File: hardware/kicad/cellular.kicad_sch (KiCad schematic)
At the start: 41 parts, among them J4 SMN-304, Q3 S8050, Q4 S8050, Q5 PMBT3904, Q6 PMBT3904, U9 A7670C

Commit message: GNSS and Antenna Update
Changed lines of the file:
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@@
-	(wire
-		(pts
-			(xy 178.435 20.955) (xy 181.61 20.955)
-		)
-		(stroke
-			(width 0)
-			(type default)
-		)
-	)
 	(wire
 		(pts
@@
 	(wire
 		(pts
-			(xy 181.61 20.955) (xy 181.61 30.48)
+			(xy 181.61 22.86) (xy 181.61 30.48)
 		)
 		(stroke
@@
 	(hierarchical_label "CELL_BATT"
 		(shape input)
-		(at 178.435 20.955 180)
-		(fields_autoplaced yes)
-		(effects
+		(at 181.61 22.86 180)
+		(fields_autoplaced yes)
+		(effects

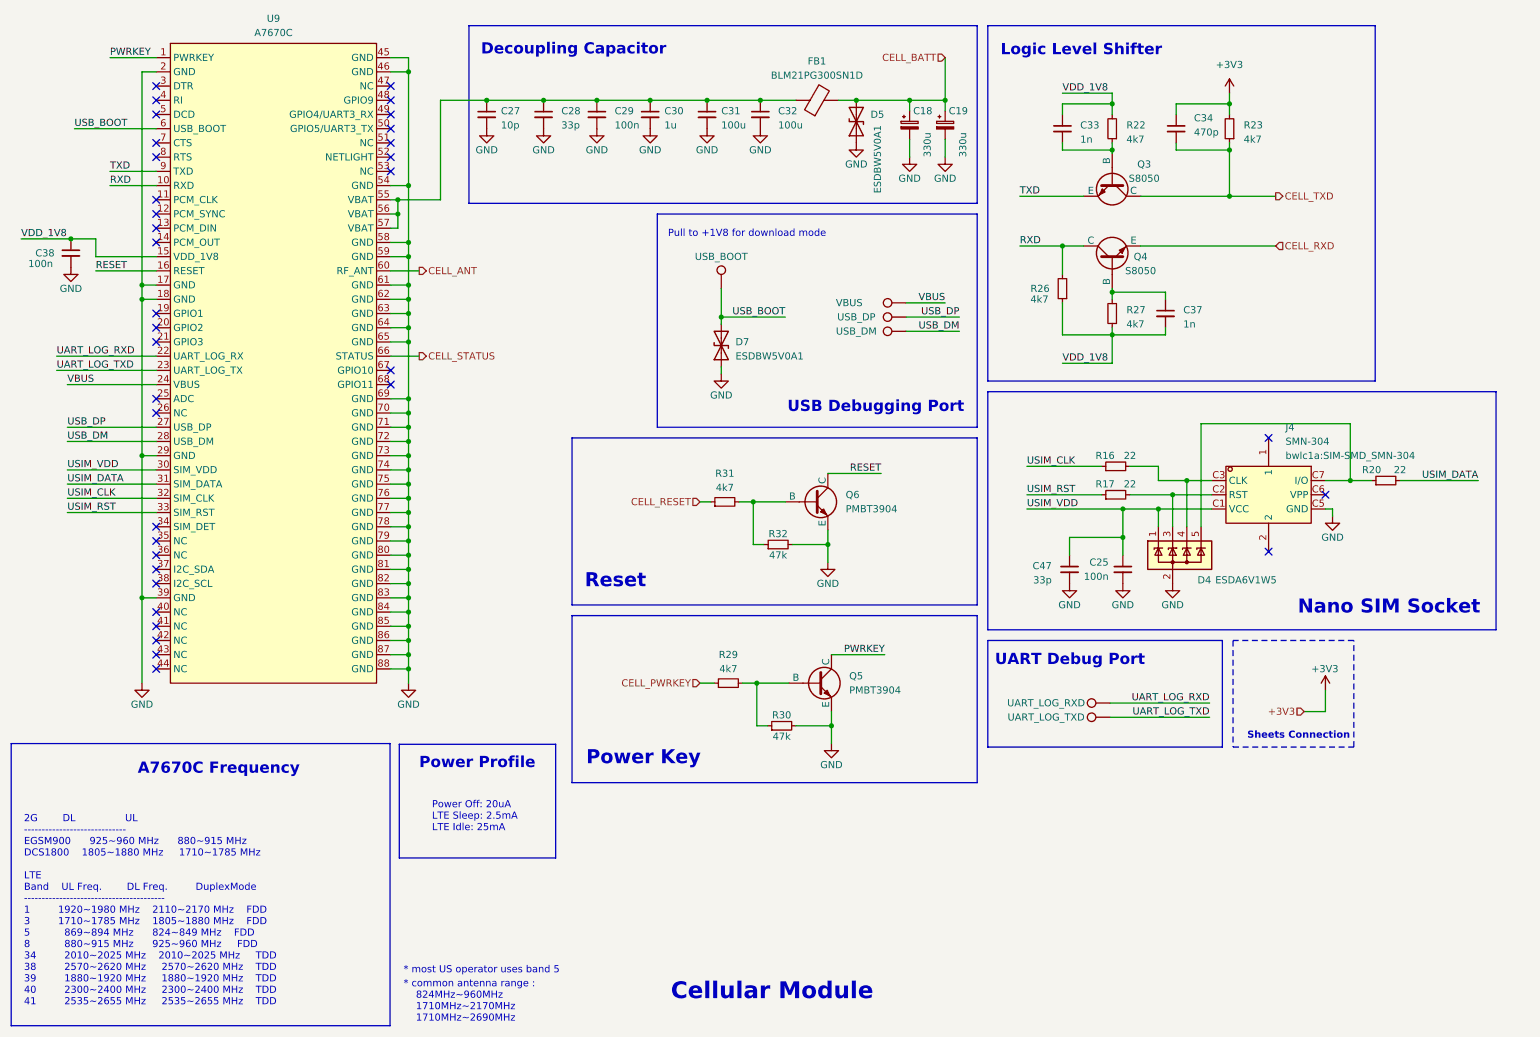
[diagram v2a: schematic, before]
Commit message: Update Sch for GNSS and main controller
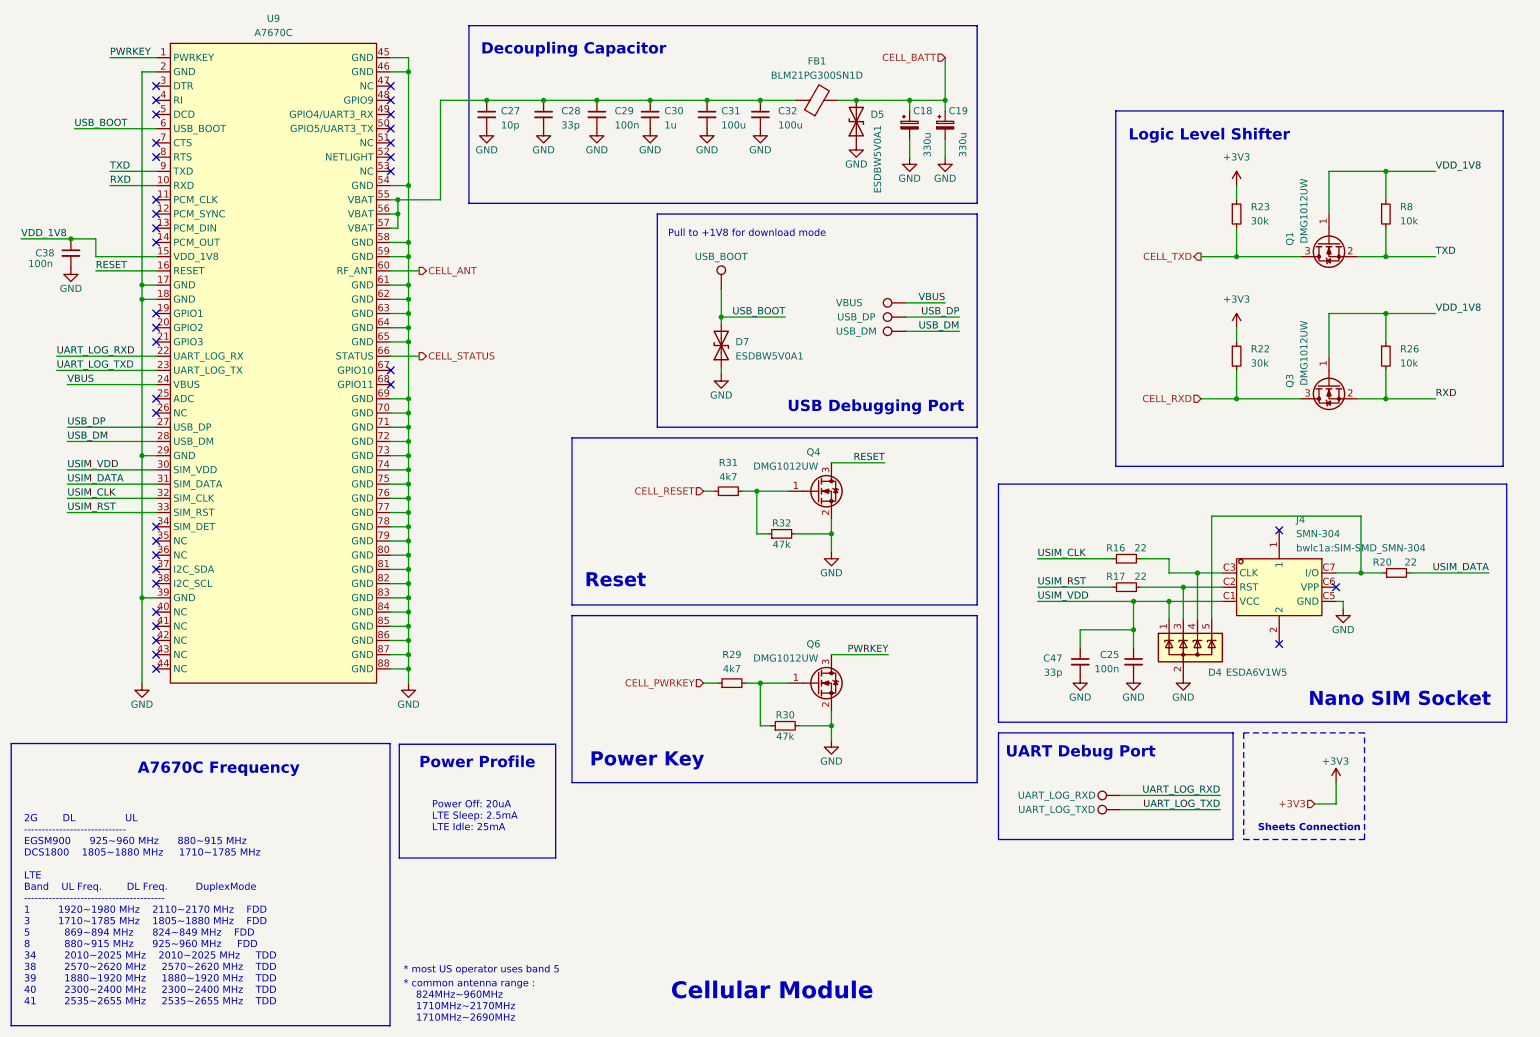
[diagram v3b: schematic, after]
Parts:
- removed C33, C37: 1n, Capacitor_SMD:C_0402_1005Metric, symbol Device:C_Small
- removed C34: 470p, Capacitor_SMD:C_0402_1005Metric, symbol Device:C_Small
- removed Q3, Q4: S8050, Package_TO_SOT_SMD:SOT-23, symbol Simulation_SPICE:NPN
- removed Q5, Q6: PMBT3904, Package_TO_SOT_SMD:SOT-23, symbol Simulation_SPICE:NPN
- removed R27: 4k7, Resistor_SMD:R_0402_1005Metric, symbol Device:R_Small
- added Q1, Q3, Q4, Q6: DMG1012UW, Package_TO_SOT_SMD:SOT-323_SC-70, symbol Device:Q_NMOS_GSD
- added R8: 10k, symbol Device:R_Small
- R22, R23: value 4k7 -> 30k; footprint Resistor_SMD:R_0402_1005Metric -> (none); Distributor LCSC -> (none); Distributor Link https://www.lcsc.com/product-detail/Chip-Resistor-Surface-M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 -> (none); Distributor Part Number C25940 -> (none); Manufacturer UNI-ROYAL(Uniroyal Elec) -> (none); Manufacturer Part Number 0402WGJ0472TCE -> (none)
- R26: value 4k7 -> 10k; footprint Resistor_SMD:R_0402_1005Metric -> (none); Distributor LCSC -> (none); Distributor Link https://www.lcsc.com/product-detail/Chip-Resistor-Surface-M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 -> (none); Distributor Part Number C25940 -> (none); Manufacturer UNI-ROYAL(Uniroyal Elec) -> (none); Manufacturer Part Number 0402WGJ0472TCE -> (none)
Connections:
- net +3V3: now also R22.1, R23.1; no longer R23.2
- net CELL_RXD: now also R22.2, Q3.3 (D)
- net CELL_TXD: now also R23.2, Q1.3 (D); no longer R23.1
- net GND: now also Q4.2 (S), Q6.2 (S)
- net PWRKEY: now also Q6.3 (D)
- net RESET: now also Q4.3 (D)
- net RXD: now also Q3.2 (S)
- net TXD: now also Q1.2 (S), R8.2
- net VDD_1V8: now also Q1.1 (G), Q3.1 (G), R8.1; no longer R22.2
- net at R31.2, R32.1: now also Q4.1 (G)
- net at R29.2, R30.1: now also Q6.1 (G)
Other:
- moved on the sheet: C25, C47, D4, J4, R16, R17, R20, R29, R30, R31, R32

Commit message: Update for PCB Layout
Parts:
- R1: renamed from R23; footprint (none) -> Resistor_SMD:R_0402_1005Metric
- R2: renamed from R8; footprint (none) -> Resistor_SMD:R_0402_1005Metric
- R3: renamed from R22; footprint (none) -> Resistor_SMD:R_0402_1005Metric
- R4: renamed from R26; footprint (none) -> Resistor_SMD:R_0402_1005Metric
- renumbered C27 to C1, C47 to C10, C25 to C11, C28 to C2, C29 to C3, C30 to C4, C31 to C5, C32 to C6, C18 to C7, C19 to C8, C38 to C9, D5 to D1, D7 to D2, D4 to D3, J4 to J1, Q3 to Q2, Q4 to Q3, Q6 to Q4, R29 to R10, R30 to R11, R31 to R5, R32 to R6, R16 to R7, R20 to R8, R17 to R9, TP11 to TP1, TP3 to TP2, TP1 to TP3, TP2 to TP4, TP4 to TP5, TP12 to TP6, U9 to U1

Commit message: Finish Manufacturing File
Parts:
- Q1, Q2, Q3, Q4: value DMG1012UW -> 2N7002; footprint Package_TO_SOT_SMD:SOT-323_SC-70 -> Package_TO_SOT_SMD:SOT-23; Distributor Link https://www.lcsc.com/product-detail/MOSFETs_Diodes-Incorporated-DMG1012UW-7_C156390.html -> https://www.lcsc.com/product-detail/MOSFETs_Diodes-Incorporated-2N7002H-7_C150714.html; Distributor Part Number C156390 -> C150714; Manufacturer Diodes Incorporated -> Diodes Incorporated; Manufacturer Part Number DMG1012UW-7 -> 2N7002H-7
- R1, R3: Distributor (none) -> LCSC; Distributor Link (none) -> https://www.lcsc.com/product-detail/Chip-Resistor-Surface-M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; Distributor Part Number (none) -> C25776; Manufacturer (none) -> UNI-ROYAL(Uniroyal Elec); Manufacturer Part Number (none) -> 0402WGF3002TCE
- R2, R4: Distributor (none) -> LCSC; Distributor Link (none) -> https://www.lcsc.com/product-detail/Chip-Resistor-Surface-M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; Distributor Part Number (none) -> C25744; Manufacturer (none) -> UNI-ROYAL(Uniroyal Elec); Manufacturer Part Number (none) -> 0402WGF1002TCE
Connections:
- net CELL_RXD: now also Q2.2 (S); no longer Q2.3 (D)
- net CELL_TXD: now also Q1.2 (S); no longer Q1.3 (D)
- net RXD: now also Q2.3 (D); no longer Q2.2 (S)
- net TXD: now also Q1.3 (D); no longer Q1.2 (S)
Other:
- moved on the sheet: C10, C11, D3, J1, R1, R2, R3, R4, R7, R8, R9

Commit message: update
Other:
- note added: "TODO: re-check mosfet"
- note added: "TODO: re-check mosfet resistor value"
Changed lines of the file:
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@@
+		)
+	)
+	(text "TODO: re-check mosfet resistor value"
+		(exclude_from_sim no)
+		(at 111.506 137.668 90)
+		(effects
+			(font
+				(size 2 2)
+				(thickness 0.254)
+				(bold yes)
+			)
+			(justify left bottom)
 		)
 	)
@@
 				(bold yes)
 			)
+			(justify left bottom)
+		)
+	)
+	(text "TODO: re-check mosfet"
+		(exclude_from_sim no)
+		(at 192.532 29.972 0)
+		(effects
+			(font
+				(size 2 2)
+				(thickness 0.254)
+				(bold yes)
+			)

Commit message: Minor change in layout and added GND test point
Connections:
- net CELL_RXD: now also Q2.3 (D); no longer Q2.2 (S)
- net CELL_TXD: now also Q1.3 (D); no longer Q1.2 (S)
- net RXD: now also Q2.2 (S); no longer Q2.3 (D)
- net TXD: now also Q1.2 (S); no longer Q1.3 (D)
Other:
- moved on the sheet: Q1, Q2
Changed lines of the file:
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@@
 	(symbol
 		(lib_id "Device:Q_NMOS_GSD")
-		(at 229.87 81.28 270)
+		(at 229.87 81.28 90)
+		(mirror x)
 		(unit 1)
 		(exclude_from_sim no)
@@
 		(on_board yes)
 		(dnp no)
-		(fields_autoplaced yes)
 		(property "Reference" "Q2"
 			(at 229.87 87.63 90)
@@
 		)
 		(property "Footprint" "Package_TO_SOT_SMD:SOT-23"
-			(at 232.41 86.36 0)
+			(at 227.33 86.36 0)
 			(effects
 				(font
@@
 	(symbol
 		(lib_id "Device:Q_NMOS_GSD")
-		(at 229.87 55.88 270)
+		(at 229.87 55.88 90)
+		(mirror x)
 		(unit 1)
 		(exclude_from_sim no)
@@
 		(on_board yes)
 		(dnp no)
-		(fields_autoplaced yes)
 		(property "Reference" "Q1"
 			(at 229.87 62.23 90)
@@
 		)
 		(property "Footprint" "Package_TO_SOT_SMD:SOT-23"
-			(at 232.41 60.96 0)
-			(effects
-				(font
+			(at 227.33 60.96 0)
+			(effects
+				(font

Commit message: Update Production File
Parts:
- removed Q1, Q2, Q3, Q4: 2N7002, Package_TO_SOT_SMD:SOT-23, symbol Device:Q_NMOS_GSD
- removed R1, R3: 30k, Resistor_SMD:R_0402_1005Metric, symbol Device:R_Small
- removed R10, R5: 4k7, Resistor_SMD:R_0402_1005Metric, symbol Device:R_Small
- removed R11, R6: 47k, Resistor_SMD:R_0402_1005Metric, symbol Device:R_Small
- removed R2, R4: 10k, Resistor_SMD:R_0402_1005Metric, symbol Device:R_Small
- added C12, C13: 100n, Capacitor_SMD:C_0402_1005Metric, symbol Device:C_Small
- added U2: TXB0104RGY, Package_DFN_QFN:Texas_S-PVQFN-N14, symbol Logic_LevelTranslator:TXB0104RGY
- D2: renamed from D3; Distributor Link https://www.lcsc.com/product-detail/span-style-background-color-ff0-ESD-span-Protection-Devices_TECH-PUBLIC-ESDA6V1W5-TP_C970036.html -> https://www.lcsc.com/product-detail/span-style-background-color-ff0-ESD-span-and-Surge-Protection-TVS-span-style-background-color-ff0-ESD-span_TECH-PUBLIC-ESDA6V1W5_C3040609.html; Distributor Part Number C970036 -> C3040609; Manufacturer Part Number ESDA6V1W5-TP -> ESDA6V1W5
- U1: value A7670C -> A7670G-LABE; Distributor Link https://www.lcsc.com/product-detail/2G-3G-4G-5G-Modules_SIMCom-Wireless-Solutions-A7670C-MASL_C2891912.html -> https://www.lcsc.com/product-detail/2G-3G-4G-5G-Modules_SIMCom-Wireless-Solutions-A7670G-LABE_C22462360.html; Distributor Part Number C2891912 -> C22462360; Manufacturer Part Number A7670C-MASL -> A7670G-LABE
- renumbered C11 to C10, C9 to C11, C10 to C9, D2 to D3, R7 to R1, R8 to R2, R9 to R3
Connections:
- net +3V3: now also C13.1, U2.14 (VCCB)
- net CELL_PWRKEY: now also U2.13 (B1)
- net CELL_RESET: now also U2.10 (B4)
- net CELL_RXD: now also U2.11 (B3)
- net CELL_TXD: now also U2.12 (B2)
- net GND: now also C12.1, C13.2, U2.15 (Pad), U2.7 (GND)
- net PWRKEY: now also U2.2 (A1)
- net RESET: now also U2.5 (A4)
- net RXD: now also U2.4 (A3)
- net TXD: now also U2.3 (A2)
- net VDD_1V8: now also C12.2, U2.1 (VCCA), U2.8 (OE)
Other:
- note added: "*RESET and PWRKEY are internally pull-up with 50k ohm resistor"
- note added: "Make sure pull-up/pull-down above 50k ohm to ensure that they do not contend with output driver"
- note added: "make sure Vcca <= Vccb"
- note removed: "Logic Level Shifter"
- note removed: "Power Key"
- note removed: "Reset"
- note removed: "TODO: re-check mosfet"
- note removed: "TODO: re-check mosfet resistor value"
- moved on the sheet: C10, C9, D2, J1, R1, R2, R3
